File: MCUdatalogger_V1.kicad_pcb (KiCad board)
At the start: 2 copper layers, 29 parts, among them J1 Conn_01x04_Pin, J2 Conn_01x04_Pin, J3 Conn_01x09_Pin, J4 Conn_02x03_Odd_Even, U1 24LC1025, U2 DS1337S+, U3 24LC1025, U4 ATMEGA328P-AU, Y1 32.768 KHz, Y2 16 MHz

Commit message: Connections established
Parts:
- moved H3 46.4 mm to (123.7, 46.8)
- moved H4 44.8 mm to (123.7, 73.4)
- moved J2 37.7 mm to (83.9, 73.7), turned to 90 degrees
- moved R5 32.9 mm to (116.2, 50.9), turned to 180 degrees
- moved R6 32.6 mm to (116.2, 54.9)
- moved R7 30.5 mm to (111.3, 51.0)
- moved J3 27.8 mm to (109.2, 73.7), turned to 90 degrees
- moved R3 27.5 mm to (111.3, 60.2)
- moved Y1 27.3 mm to (80.0, 64.8), turned to 90 degrees
- moved R4 26.8 mm to (111.3, 55.7), turned to 180 degrees
- moved C5 26.7 mm to (106.9, 47.4)
- moved R1 20.8 mm to (85.7, 68.6)
- moved C3 20.1 mm to (101.9, 47.4)
- moved H2 18.7 mm to (78.7, 73.7)
- moved R2 18.5 mm to (89.5, 68.6), turned to 180 degrees
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- renumbered J3 to J2, J2 to J3
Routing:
- net /VCC: track 0.00 -> 137.1 mm, vias 0 -> 2
- net /SCK: track 0.00 -> 100.2 mm, vias 0 -> 4
- net /SDA: track 0.00 -> 68.1 mm, vias 0 -> 3
- net GND: track 0.00 -> 67.0 mm, vias 0 -> 10
- net Net-(BT1-+): track 0.00 -> 60.8 mm, vias 0 -> 3
- net /RESET: track 0.00 -> 35.5 mm, vias 0 -> 2
- net /TX: track 0.00 -> 32.1 mm, vias 0 -> 1
- net Net-(U4-PB7): track 0.00 -> 30.8 mm, vias 0 -> 4
- net /RX: track 0.00 -> 30.1 mm, vias 0 -> 1
- net /D2: track 0.00 -> 28.1 mm, vias 0 -> 1
- net Net-(U4-PB6): track 0.00 -> 28.0 mm
- net /D3: track 0.00 -> 27.8 mm
- net /MISO: track 0.00 -> 26.4 mm, vias 0 -> 1
- net /MOSI: track 0.00 -> 26.3 mm
- net /D4: track 0.00 -> 23.4 mm
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
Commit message: PCB Ready
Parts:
- added REF: KiCad-Logo2_5mm_SilkScreen, Symbol:KiCad-Logo2_5mm_SilkScreen, B.Cu at (113.1, 48.4)
- R1: value 10 K -> 10K
- moved H3 0.28 mm to (123.6, 47.0)
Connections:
- BT1 pad 1: Net-(BT1-+) -> /VCC
- C5 pad 1: Net-(BT1-+) -> /VCC
- D2 pad 2: Net-(BT1-+) -> /VCC
- U4 pad 18: Net-(BT1-+) -> /VCC
- U4 pad 4: Net-(BT1-+) -> /VCC
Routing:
- net /VCC: track 137.1 -> 218.4 mm, vias 2 -> 7
- net Net-(BT1-+): track 60.8 -> 0.00 mm, vias 3 -> 0
- net GND: track 67.0 -> 112.8 mm, vias 10 -> 13
- net /D8: track 13.8 -> 18.8 mm
- net /D7: track 14.4 -> 16.7 mm
- net /SCK: track 100.2 -> 99.2 mm
- added copper zone on F.Cu, net /VCC
- added copper zone on B.Cu, net GND
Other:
- board outline added: 52.4 x 33.8 mm
- board text added: "- 2Mbit EEPROM - RTC - I2C, SPI, GPIOs"
- board text added: "0.0000 mm / 0.0000 mm"
- board text added: "0.3000 mm"
- board text added: "1.6000 mm"
- board text added: "2"
- board text added: "3"
- board text added: "4"
- board text added: "5"
- board text added: "52.3610 mm x 33.7790 mm"
- board text added: "6"
- board text added: "7"
- board text added: "8"
- board text added: "BOARD CHARACTERISTICS"
- board text added: "Board Thickness:"
- board text added: "Board overall dimensions:"
- board text added: "Castellated pads:"
- board text added: "Copper Finish:"
- board text added: "Copper Layer Count:"
- board text added: "Data logger with The ATMega328P."
- board text added: "Edge card connectors:"
- board text added: "GND"
- board text added: "I2C"
- board text added: "ICSP"
- board text added: "ICSP MISO | VCC SCK | MOSI RESET| GND"
- board text added: "Impedance Control:"
- board text added: "Min hole diameter:"
- board text added: "Min track/spacing:"
- board text added: "No"
- board text added: "None"
- board text added: "Plated Board Edge:"
- board text added: "RX"
- board text added: "SCK"
- board text added: "SDA"
- board text added: "SERIAL"
- board text added: "TX"
- board text added: "VCC"

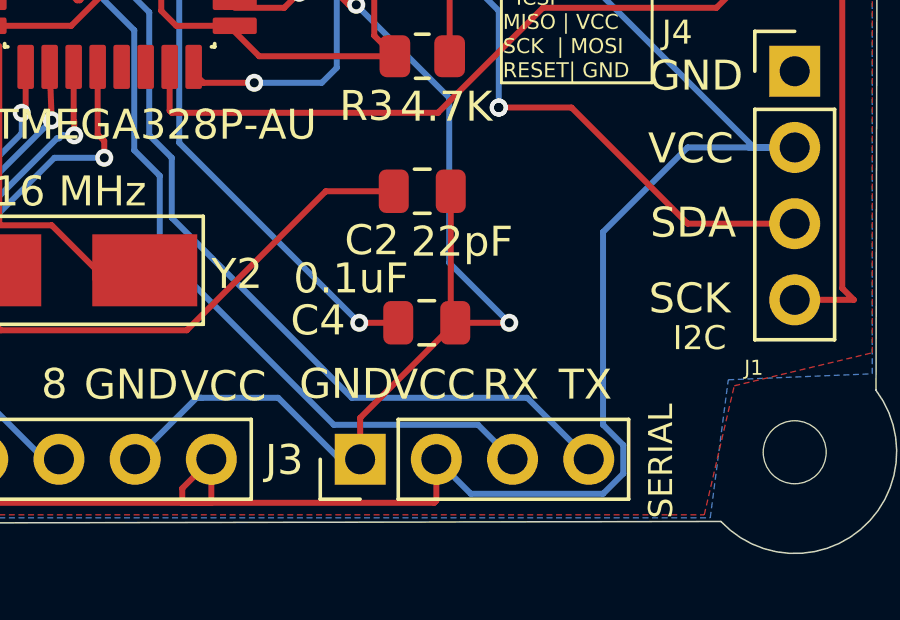
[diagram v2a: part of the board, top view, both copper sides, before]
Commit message: 3D View updated
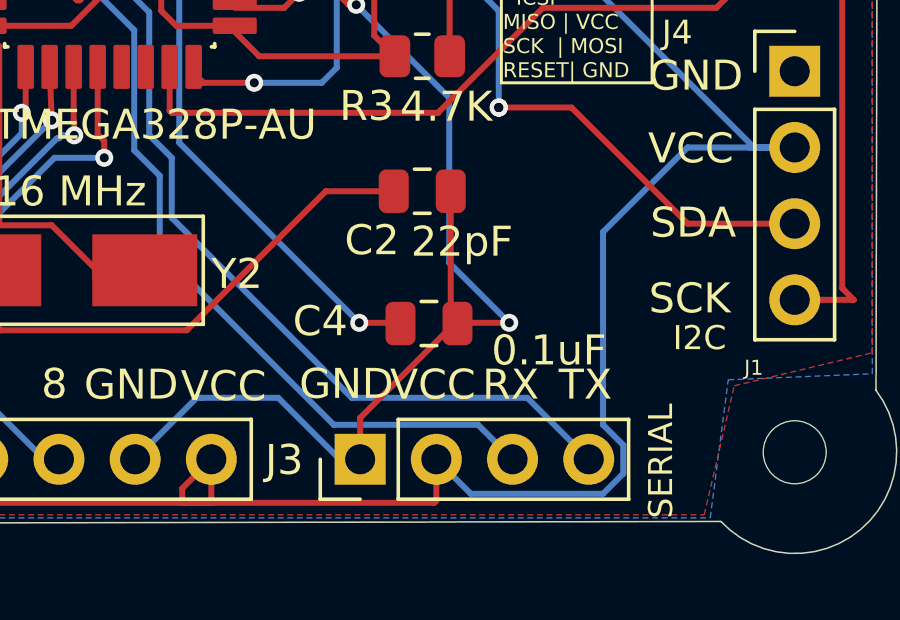
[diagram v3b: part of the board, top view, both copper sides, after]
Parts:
- moved C4 0.08 mm to (111.5, 69.1)
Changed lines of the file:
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@@
     (pad "8" smd roundrect (at 3.6 -1.905) (size 1.6 0.6) (layers "F.Cu" "F.Paste" "F.Mask") (roundrect_rratio 0.25)
       (net 2 "/VCC") (pinfunction "VCC") (pintype "power_in"))
-    (model "${KICAD6_3DMODEL_DIR}/Package_SO.3dshapes/SOIC-8_5.23x5.23mm_P1.27mm.wrl"
+    (model ":KICAD7_3DMODEL_DIR:Package_SO.3dshapes/SO-8_3.9x4.9mm_P1.27mm.wrl"
       (offset (xyz 0 0 0))
       (scale (xyz 1 1 1))
@@
   )
   (footprint "Capacitor_SMD:C_0805_2012Metric" (layer "F.Cu")
-    (at 111.44 69.11 180)
+    (at 111.515 69.135 180)
     (descr "Capacitor SMD 0805 (2012 Metric), square (rectangular) end terminal, IPC_7351 nominal, (Body size source: IPC-SM-782 page 76, https://www.pcb-3d.com/wordpress/wp-content/uploads/ipc-sm-782a_amendment_1_and_2.pdf, https://docs.google.com/spreadsheets/d/1BsfQQcO9C6DZCsRaXUlFlo91Tg2WpOkGARC1WS5S8t0/edit?usp=sharing), generated with kicad-footprint-generator")
     (tags "capacitor")
@@
         (effects (font (size 1 1) (thickness 0.15)))
     )
-    (fp_text value "0.1uF" (at 2.525 1.475) (layer "F.SilkS")
+    (fp_text value "0.1uF" (at -4 -0.9) (layer "F.SilkS")
         (effects (font (size 1 1) (thickness 0.15)))
     )
@@
     (pad "2" smd rect (at 2.6 0 180) (size 3.5 2.4) (layers "F.Cu" "F.Paste" "F.Mask")
       (net 3 "Net-(U4-PB6)") (pinfunction "2") (pintype "passive"))
-    (model "${KICAD6_3DMODEL_DIR}/Crystal.3dshapes/Crystal_SMD_5032-2Pin_5.0x3.2mm_HandSoldering.wrl"
+    (model ":KICAD7_3DMODEL_DIR:Crystal.3dshapes/Crystal_SMD_0603-2Pin_6.0x3.5mm.step"
       (offset (xyz 0 0 0))
       (scale (xyz 1 1 1))
@@
     (pad "32" smd roundrect (at -2.8 -4.17) (size 0.55 1.47) (layers "F.Cu" "F.Paste" "F.Mask") (roundrect_rratio 0.125)
       (net 12 "/D2") (pinfunction "PD2") (pintype "bidirectional") (solder_mask_margin 0.102))
+    (model ":KICAD7_3DMODEL_DIR:Package_QFP.3dshapes/TQFP-32_7x7mm_P0.8mm.step"
+      (offset (xyz 0 0 0))
+      (scale (xyz 1 1 1))
+      (rotate (xyz 0 0 0))
+    )
   )
   (footprint "Connector_PinHeader_2.54mm:PinHeader_1x04_P2.54mm_Vertical" (layer "F.Cu")
@@
     (pad "8" smd roundrect (at 2.475 -1.905) (size 1.97 0.59) (layers "F.Cu" "F.Paste" "F.Mask") (roundrect_rratio 0.125)
       (net 2 "/VCC") (pinfunction "VCC") (pintype "power_in") (solder_mask_margin 0.102))
+    (model ":KICAD7_3DMODEL_DIR:Package_SO.3dshapes/SO-8_3.9x4.9mm_P1.27mm.wrl"
+      (offset (xyz 0 0 0))
+      (scale (xyz 1 1 1))
+      (rotate (xyz 0 0 0))
+    )
   )
   (footprint "Package_SO:SOIC-8_5.23x5.23mm_P1.27mm" (layer "F.Cu")
@@
     (pad "8" smd roundrect (at 3.6 -1.905) (size 1.6 0.6) (layers "F.Cu" "F.Paste" "F.Mask") (roundrect_rratio 0.25)
       (net 2 "/VCC") (pinfunction "VCC") (pintype "power_in"))
-    (model "${KICAD6_3DMODEL_DIR}/Package_SO.3dshapes/SOIC-8_5.23x5.23mm_P1.27mm.wrl"
+    (model ":KICAD7_3DMODEL_DIR:Package_SO.3dshapes/SO-8_3.9x4.9mm_P1.27mm.wrl"
       (offset (xyz 0 0 0))
       (scale (xyz 1 1 1))
@@
     (pad "2" smd rect (at 2.6 0 90) (size 3.5 2.4) (layers "F.Cu" "F.Paste" "F.Mask")
       (net 24 "Net-(U2-X1)") (pinfunction "2") (pintype "passive"))
-    (model "${KICAD6_3DMODEL_DIR}/Crystal.3dshapes/Crystal_SMD_5032-2Pin_5.0x3.2mm_HandSoldering.wrl"
-      (offset (xyz 0 0 0))
-      (scale (xyz 1 1 1))
+    (model ":KICAD7_3DMODEL_DIR:Crystal.3dshapes/Crystal_SMD_0603-2Pin_6.0x3.5mm.step"
+      (offset (xyz 0 0 0))
+      (scale (xyz 1 1 1))
